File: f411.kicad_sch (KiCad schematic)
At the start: 16 parts, among them J18 THTPad, J21 Conn_01x04_Pin, SW1 SW_Push, SW2 SW_Push, U5 STM32F411CEUx

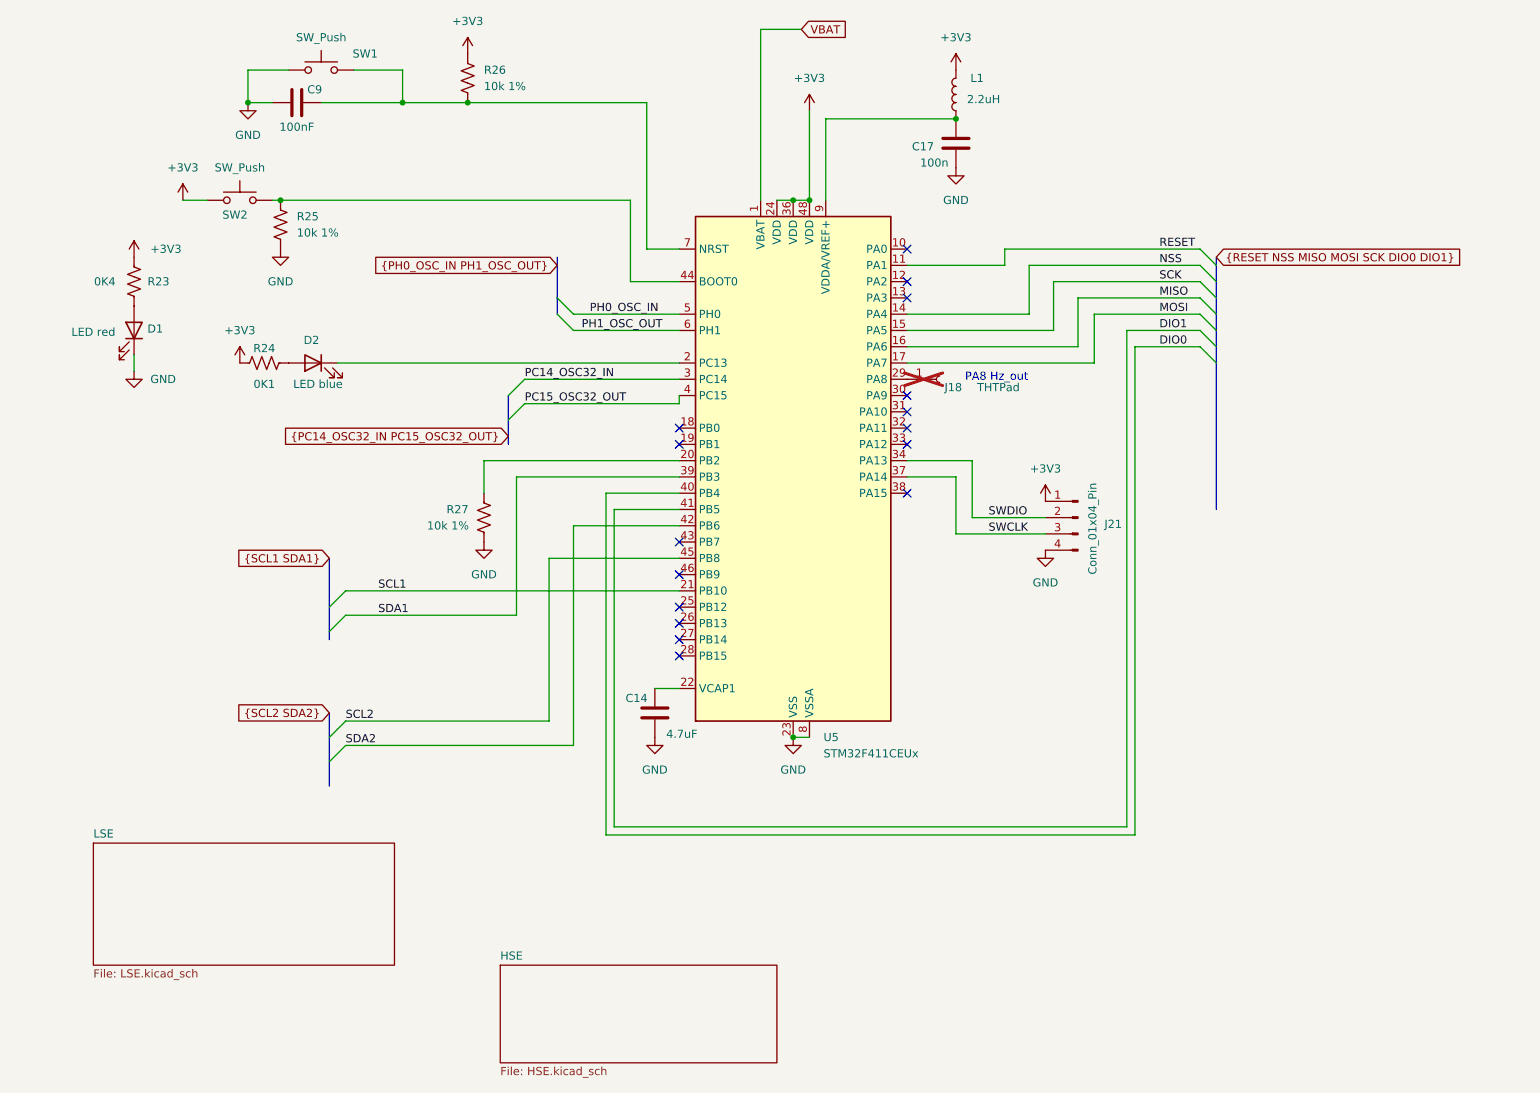
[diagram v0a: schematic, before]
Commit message: layout with F411 roughly good but needs work.
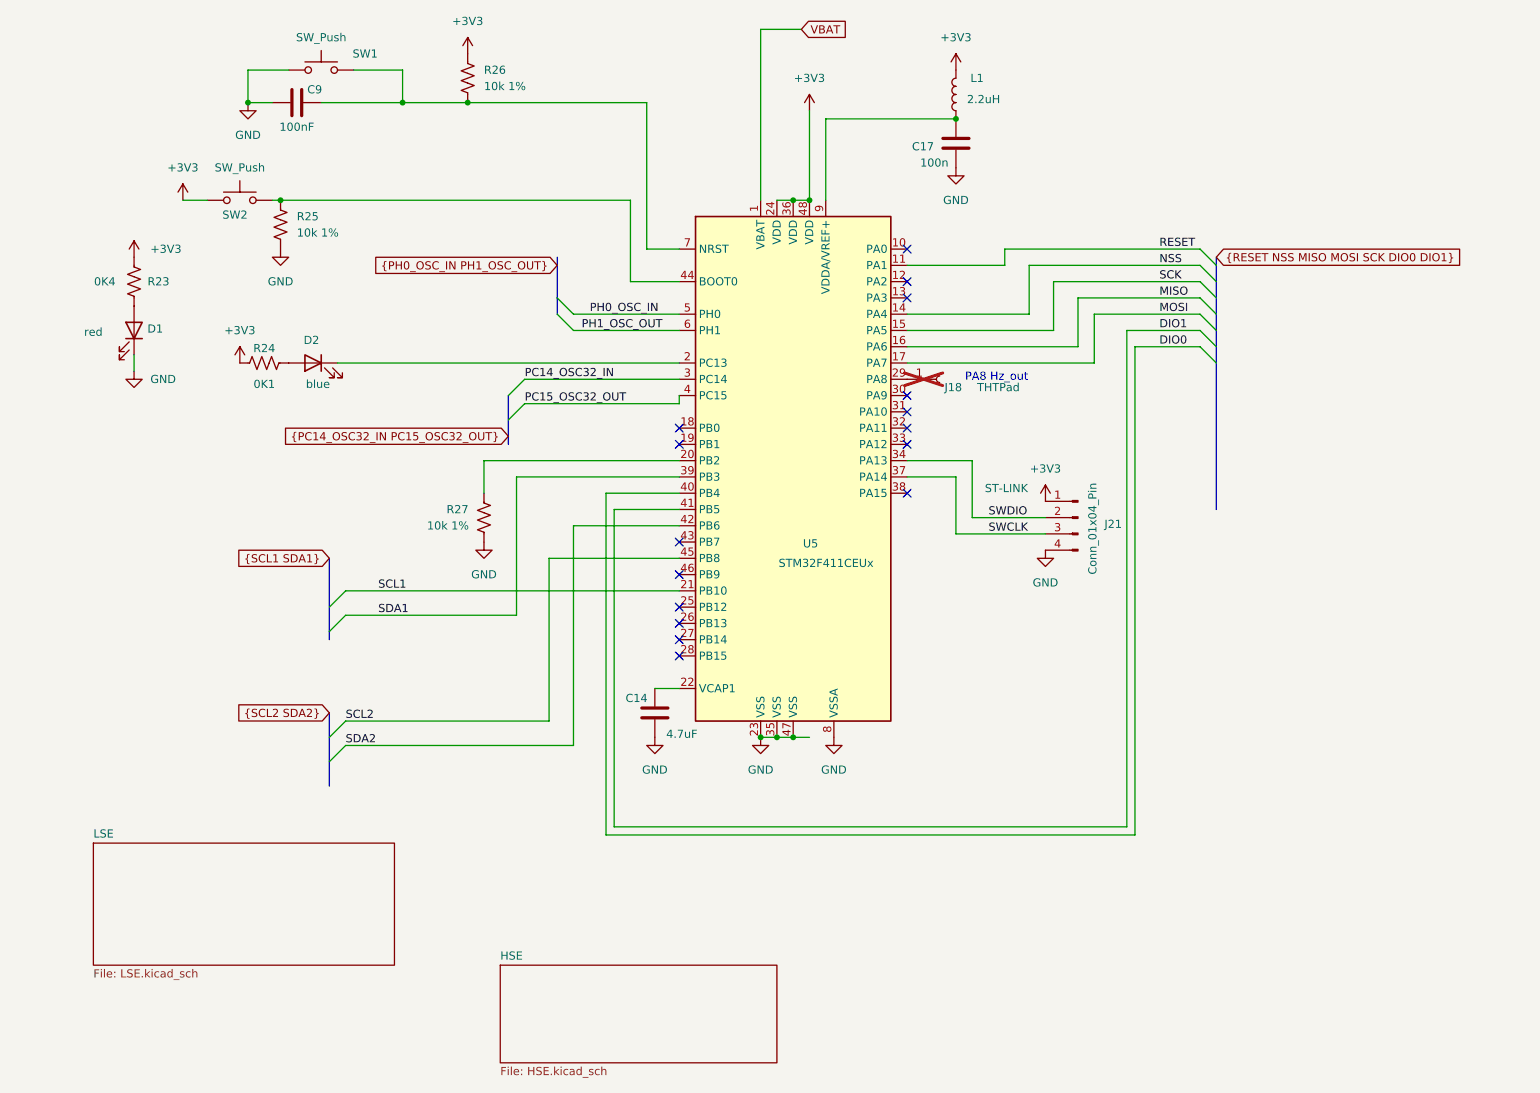
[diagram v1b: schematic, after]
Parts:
- C14, C17, C9: footprint ProjectLib:C_0805_2012Metric -> ProjectLib:C_0603_1608Metric
- D1: value LED red -> red
- D2: value LED blue -> blue
- J21: footprint ProjectLib:JST_XH_B4B-XH-A_1x04_P2.50mm_Vertical -> ProjectLib:PinSocket_2x02_P2.54mm_Vertical; Note (none) -> ST-LINK
- U5: footprint Package_DFN_QFN:QFN-48-1EP_7x7mm_P0.5mm_EP5.6x5.6mm -> ProjectLib:QFN-48-1EP_7x7mm_P0.5mm_EP5.6x5.6mm; Manufacturer (none) -> STM; MfgPart (none) -> STM32F411CEUx
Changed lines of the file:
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@@
 	)
 	(junction
+		(at 142.24 143.51)
+		(diameter 0)
+		(color 0 0 0 0)
+	)
+	(junction
 		(at 93.98 44.45)
 		(diameter 0)
@@
 	)
 	(junction
+		(at 139.7 143.51)
+		(diameter 0)
+		(color 0 0 0 0)
+	)
+	(junction
 		(at 144.78 59.69)
 		(diameter 0)
@@
 	(wire
 		(pts
+			(xy 144.78 143.51) (xy 147.32 143.51)
+		)
+		(stroke
+			(width 0)
+			(type default)
+		)
+	)
+	(wire
+		(pts
 			(xy 172.72 100.33) (xy 172.72 109.22)
 		)
@@
 	(wire
 		(pts
+			(xy 139.7 143.51) (xy 142.24 143.51)
+		)
+		(stroke
+			(width 0)
+			(type default)
+		)
+	)
+	(wire
+		(pts
 			(xy 144.78 59.69) (xy 147.32 59.69)
 		)
@@
 	(wire
 		(pts
-			(xy 144.78 143.51) (xy 147.32 143.51)
+			(xy 74.93 144.78) (xy 110.49 144.78)
 		)
 		(stroke
@@
 		)
 	)
-	(wire
+	(bus
 		(pts
-			(xy 74.93 144.78) (xy 110.49 144.78)
+			(xy 210.82 77.47) (xy 210.82 80.01)
 		)
 		(stroke
@@
 		)
 	)
-	(bus
+	(wire
 		(pts
-			(xy 210.82 77.47) (xy 210.82 80.01)
+			(xy 142.24 143.51) (xy 144.78 143.51)
 		)
 		(stroke
@@
 			)
 		)
-		(property "Footprint" "ProjectLib:JST_XH_B4B-XH-A_1x04_P2.50mm_Vertical"
+		(property "Footprint" "ProjectLib:PinSocket_2x02_P2.54mm_Vertical"
 			(at 189.23 109.22 0)
 			(effects
@@
 			)
 		)
+		(property "Note" "ST-LINK"
+			(at 178.054 104.648 0)
+			(effects
+				(font
+					(size 1.27 1.27)
+				)
+			)
+		)
 		(pin "4"
 		)
@@
 			)
 		)
-		(property "Footprint" "ProjectLib:C_0805_2012Metric"
+		(property "Footprint" "ProjectLib:C_0603_1608Metric"
 			(at 124.1552 143.51 0)
 			(effects
@@
 			)
 		)
-		(property "Value" "LED blue"
+		(property "Value" "blue"
 			(at 70.612 88.392 0)
 			(effects
@@
 			)
 		)
-		(property "Description" "Light emitting diode"
+		(property "Description" "Light emitting diode blue"
 			(at 69.85 85.09 0)
 			(effects
@@
 	(symbol
 		(lib_id "power:GND")
+		(at 139.7 143.51 0)
+		(unit 1)
+		(exclude_from_sim no)
+		(in_bom yes)
+		(on_board yes)
+		(dnp no)
+		(fields_autoplaced yes)
+		(property "Reference" "#PWR020"
+			(at 139.7 149.86 0)
+			(effects
+				(font
+					(size 1.27 1.27)
+				)
+				(hide yes)
+			)
+		)
+		(property "Value" "GND"
+			(at 139.7 148.59 0)
+			(effects
+				(font
+					(size 1.27 1.27)
+				)
+			)
+		)
+		(property "Footprint" ""
+			(at 139.7 143.51 0)
+			(effects
+				(font
+					(size 1.27 1.27)
+				)
+				(hide yes)
+			)
+		)
+		(property "Datasheet" ""
+			(at 139.7 143.51 0)
+			(effects
+				(font
+					(size 1.27 1.27)
+				)
+				(hide yes)
+			)
+		)
+		(property "Description" "Power symbol creates a global label with name \"GND\" , ground"
+			(at 139.7 143.51 0)
+			(effects
+				(font
+					(size 1.27 1.27)
+				)
+				(hide yes)
+			)
+		)
+		(pin "1"
+		)
+		(instances
+			(project ""
+				(path "/0c2d0c14-8850-4a30-bb78-b2f40cb442ba/f12d0b95-be3f-41e2-8b41-943aec5e1edf"
+					(reference "#PWR020")
+					(unit 1)
+				)
+			)
+		)
+	)
+	(symbol
+		(lib_id "power:GND")
 		(at 59.69 44.45 0)
 		(unit 1)
@@
 			)
 		)
-		(property "Footprint" "ProjectLib:C_0805_2012Metric"
+		(property "Footprint" "ProjectLib:C_0603_1608Metric"
 			(at 71.12 43.4848 0)
 			(effects
@@
 			)
 		)
-		(property "Footprint" "ProjectLib:C_0805_2012Metric"
+		(property "Footprint" "ProjectLib:C_0603_1608Metric"
 			(at 171.1452 54.61 0)
 			(effects
@@
 		(on_board yes)
 		(dnp no)
-		(fields_autoplaced yes)
 		(property "Reference" "U5"
-			(at 149.5141 143.51 0)
+			(at 146.304 113.284 0)
 			(effects
 				(font
@@
 		)
 		(property "Value" "STM32F411CEUx"
-			(at 149.5141 146.05 0)
+			(at 142.494 116.332 0)
 			(effects
 				(font
@@
 			)
 		)
-		(property "Footprint" "Package_DFN_QFN:QFN-48-1EP_7x7mm_P0.5mm_EP5.6x5.6mm"
+		(property "Footprint" "ProjectLib:QFN-48-1EP_7x7mm_P0.5mm_EP5.6x5.6mm"
 			(at 129.54 140.97 0)
 			(effects
@@
 			)
 		)
+		(property "Manufacturer" "STM"
+			(at 144.78 102.87 0)
+			(effects
+				(font
+					(size 1.27 1.27)
+				)
+				(hide yes)
+			)
+		)
+		(property "MfgPart" "STM32F411CEUx"
+			(at 144.78 102.87 0)
+			(effects
+				(font
+					(size 1.27 1.27)
+				)
+				(hide yes)
+			)
+		)
 		(pin "49"
 		)
@@
 	(symbol
 		(lib_id "power:GND")
-		(at 144.78 143.51 0)
+		(at 151.13 143.51 0)
 		(unit 1)
 		(exclude_from_sim no)
@@
 		(fields_autoplaced yes)
 		(property "Reference" "#PWR80"
-			(at 144.78 149.86 0)
+			(at 151.13 149.86 0)
 			(effects
 				(font
@@
 		)
 		(property "Value" "GND"
-			(at 144.78 148.59 0)
+			(at 151.13 148.59 0)
 			(effects
 				(font
@@
 		)
 		(property "Footprint" ""
-			(at 144.78 143.51 0)
+			(at 151.13 143.51 0)
 			(effects
 				(font
@@
 		)
 		(property "Datasheet" ""
-			(at 144.78 143.51 0)
+			(at 151.13 143.51 0)
 			(effects
 				(font
@@
 		)
 		(property "Description" "Power symbol creates a global label with name \"GND\" , ground"
-			(at 144.78 143.51 0)
+			(at 151.13 143.51 0)
 			(effects
 				(font
@@
 			)
 		)
-		(property "Value" "LED red"
+		(property "Value" "red"
 			(at 35.56 80.264 90)
 			(effects
@@
 			)
 		)
-		(property "Description" "Light emitting diode"
+		(property "Description" "Light emitting diode red"
 			(at 41.91 80.01 0)
 			(effects

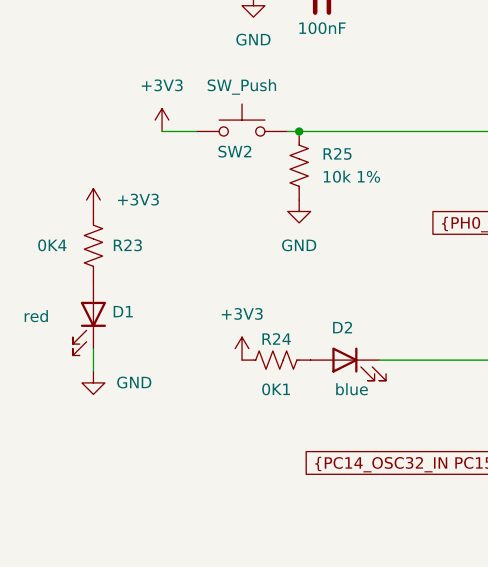
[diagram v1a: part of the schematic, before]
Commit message: Most routing done but not checked. Moat around HSE but no net-tie yet.
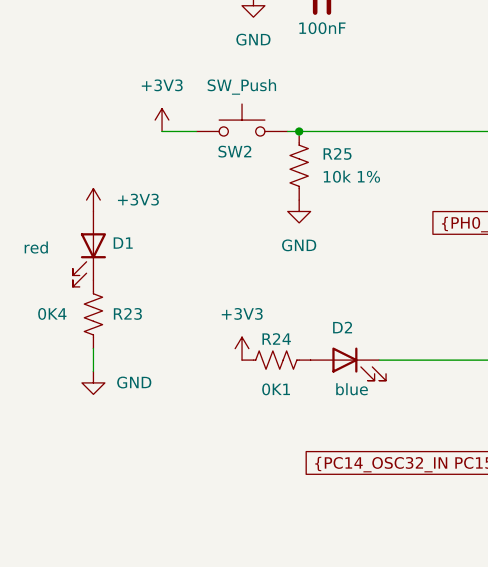
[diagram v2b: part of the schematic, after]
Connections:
- net +3V3: now also D1.2 (A); no longer R23.1
- net GND: now also R23.2; no longer D1.1 (K)
- new net: D1.1 (K), R23.1
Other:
- moved on the sheet: D1, R23
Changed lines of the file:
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@@
 	(symbol
 		(lib_id "ProjectLib:LED")
-		(at 41.91 80.01 270)
+		(at 41.91 72.39 270)
 		(mirror x)
 		(unit 1)
@@
 		(dnp no)
 		(property "Reference" "D1"
-			(at 45.212 79.756 90)
+			(at 45.212 72.136 90)
 			(effects
 				(font
@@
 		)
 		(property "Value" "red"
-			(at 35.56 80.264 90)
+			(at 35.56 72.644 90)
 			(effects
 				(font
@@
 		)
 		(property "Footprint" "ProjectLib:LED_0603_1608Metric"
-			(at 41.91 80.01 0)
+			(at 41.91 72.39 0)
 			(effects
 				(font
@@
 		)
 		(property "Datasheet" "~"
-			(at 41.91 80.01 0)
+			(at 41.91 72.39 0)
 			(effects
 				(font
@@
 		)
 		(property "Description" "Light emitting diode red"
-			(at 41.91 80.01 0)
+			(at 41.91 72.39 0)
 			(effects
 				(font
@@
 		)
 		(property "Manufacturer" "Yongyu Photoelectric"
-			(at 41.91 80.01 0)
+			(at 41.91 72.39 0)
 			(effects
 				(font
@@
 		)
 		(property "MfgPart" "yy0603re-nn1s0-t2ar4"
-			(at 41.91 80.01 0)
+			(at 41.91 72.39 0)
 			(effects
 				(font
@@
 		)
 		(property "MountType" "SMT"
-			(at 41.91 80.01 0)
+			(at 41.91 72.39 0)
 			(effects
 				(font
@@
 		)
 		(property "Notes" "or equivalent"
-			(at 41.91 80.01 0)
+			(at 41.91 72.39 0)
 			(effects
 				(font
@@
 	(symbol
 		(lib_id "ProjectLib:R_US")
-		(at 41.91 72.39 0)
+		(at 41.91 80.01 0)
 		(unit 1)
 		(exclude_from_sim no)
@@
 		(dnp no)
 		(property "Reference" "R23"
-			(at 45.72 72.39 0)
+			(at 45.72 80.01 0)
 			(effects
 				(font
@@
 		)
 		(property "Value" "0K4"
-			(at 37.338 72.39 0)
+			(at 37.338 80.01 0)
 			(effects
 				(font
@@
 		)
 		(property "Footprint" "ProjectLib:R_0603_1608Metric"
-			(at 40.132 72.39 90)
+			(at 40.132 80.01 90)
 			(effects
 				(font
@@
 		)
 		(property "Datasheet" "~"
-			(at 41.91 72.39 0)
+			(at 41.91 80.01 0)
 			(effects
 				(font
@@
 		)
 		(property "Description" "Resistor, US symbol"
-			(at 41.91 72.39 0)
+			(at 41.91 80.01 0)
 			(effects
 				(font
@@
 		)
 		(property "MountType" "SMT"
-			(at 41.91 72.39 0)
-			(effects
-				(font
+			(at 41.91 80.01 0)
+			(effects
+				(font

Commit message: battery needs work.
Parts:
- J21: value Conn_01x04_Pin -> Conn_2x02_Pin
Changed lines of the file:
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@@
 			)
 		)
-		(property "Value" "Conn_01x04_Pin"
+		(property "Value" "Conn_2x02_Pin"
 			(at 191.516 118.11 90)
 			(effects
